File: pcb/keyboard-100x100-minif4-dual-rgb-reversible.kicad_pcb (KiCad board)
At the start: 2 copper layers, 100 x 100 mm, 96 parts, among them J1 TRRS, J2 TRRS, J3 Conn_01x04_Female, U1 MiniF4, U2 SN74LVC1T45DBV

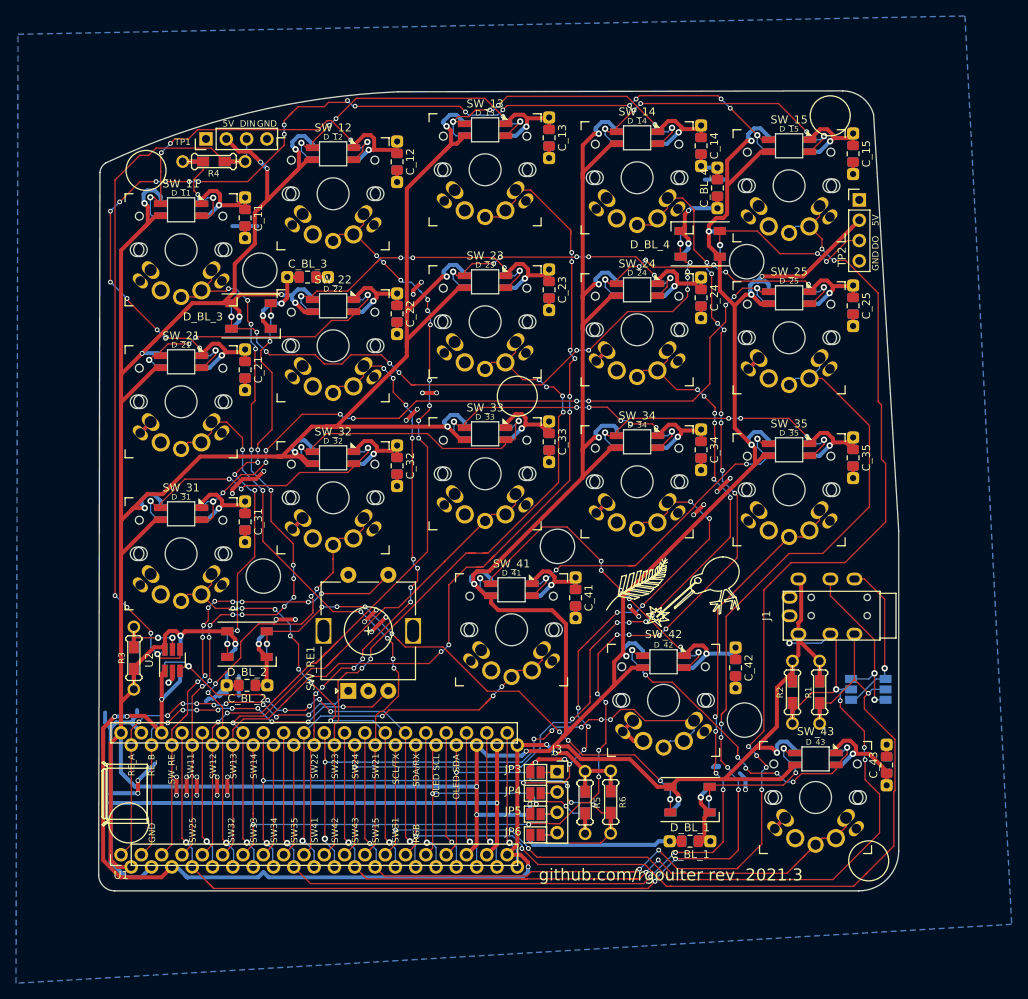
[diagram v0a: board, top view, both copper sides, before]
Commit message: Kicad: update schematic with M2 mounting holes
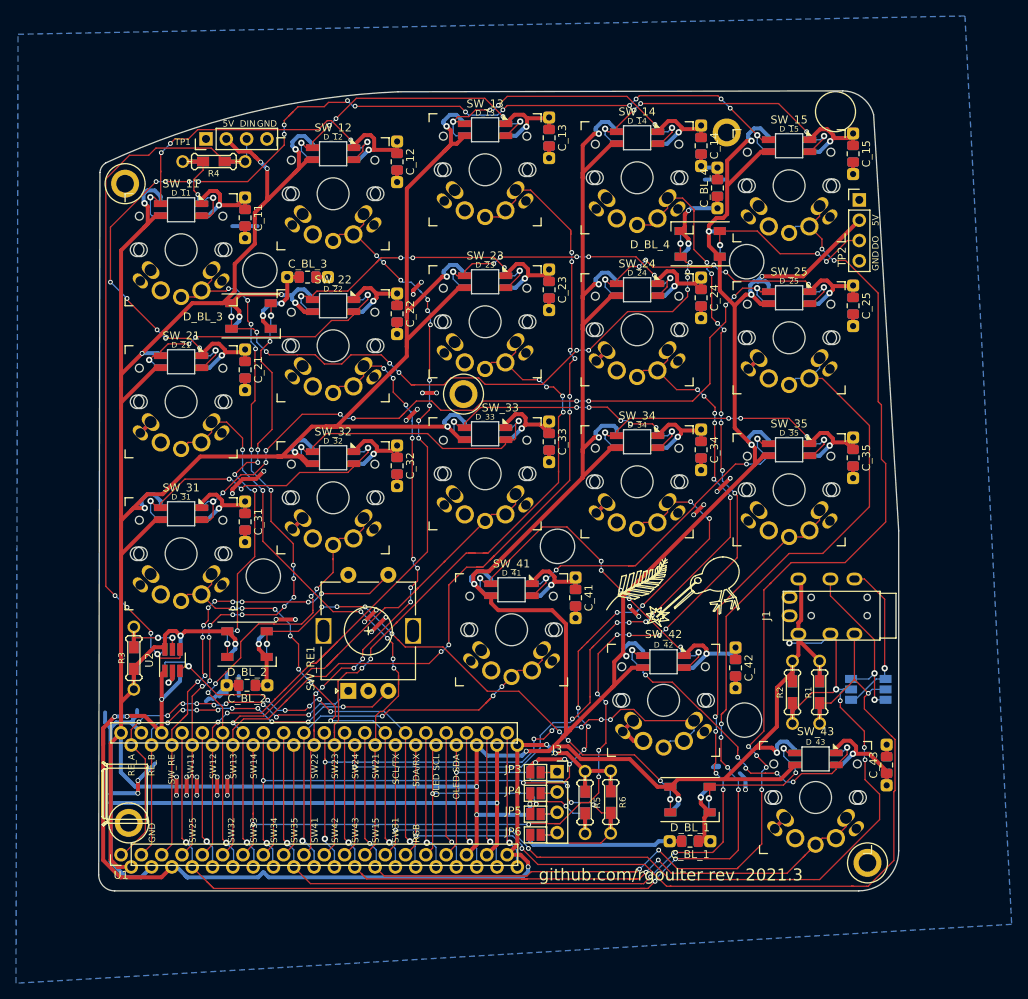
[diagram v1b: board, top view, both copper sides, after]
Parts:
- added H11: MountingHole, MountingHole:MountingHole_2.2mm_M2_ISO7380_Pad, F.Cu at (178.5, 55.2)
- added H12: MountingHole, MountingHole:MountingHole_2.2mm_M2_ISO7380_Pad, F.Cu at (103.3, 61.6)
- added H13: MountingHole, MountingHole:MountingHole_2.2mm_M2_ISO7380_Pad, F.Cu at (145.6, 87.9)
- added H14: MountingHole, MountingHole:MountingHole_2.2mm_M2_ISO7380_Pad, F.Cu at (103.8, 141.5)
- added H15: MountingHole, MountingHole:MountingHole_2.2mm_M2_ISO7380_Pad, F.Cu at (196.1, 146.5)
- moved H4 6.73 mm to (145.6, 87.9)
- moved H1 3.10 mm to (103.3, 61.6)
- moved H3 0.84 mm to (192.1, 52.6)
- moved H5 0.29 mm to (196.1, 146.5)
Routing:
- net /RGB_DIN_5V: track 86.1 -> 87.8 mm
- net /RE_A: track 47.1 -> 48.7 mm
- net /DOUT_1: track 127.1 -> 125.9 mm, vias 23 -> 21
- net /SCL_TX: track 123.8 -> 122.8 mm
- net /DOUT_2: track 95.2 -> 96.2 mm
- net /SDA_RX: track 117.9 -> 118.8 mm
- net Net-(D_BL_3-Pad4): track 79.4 -> 80.1 mm

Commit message: kicad: update keyboard for rev2021.4
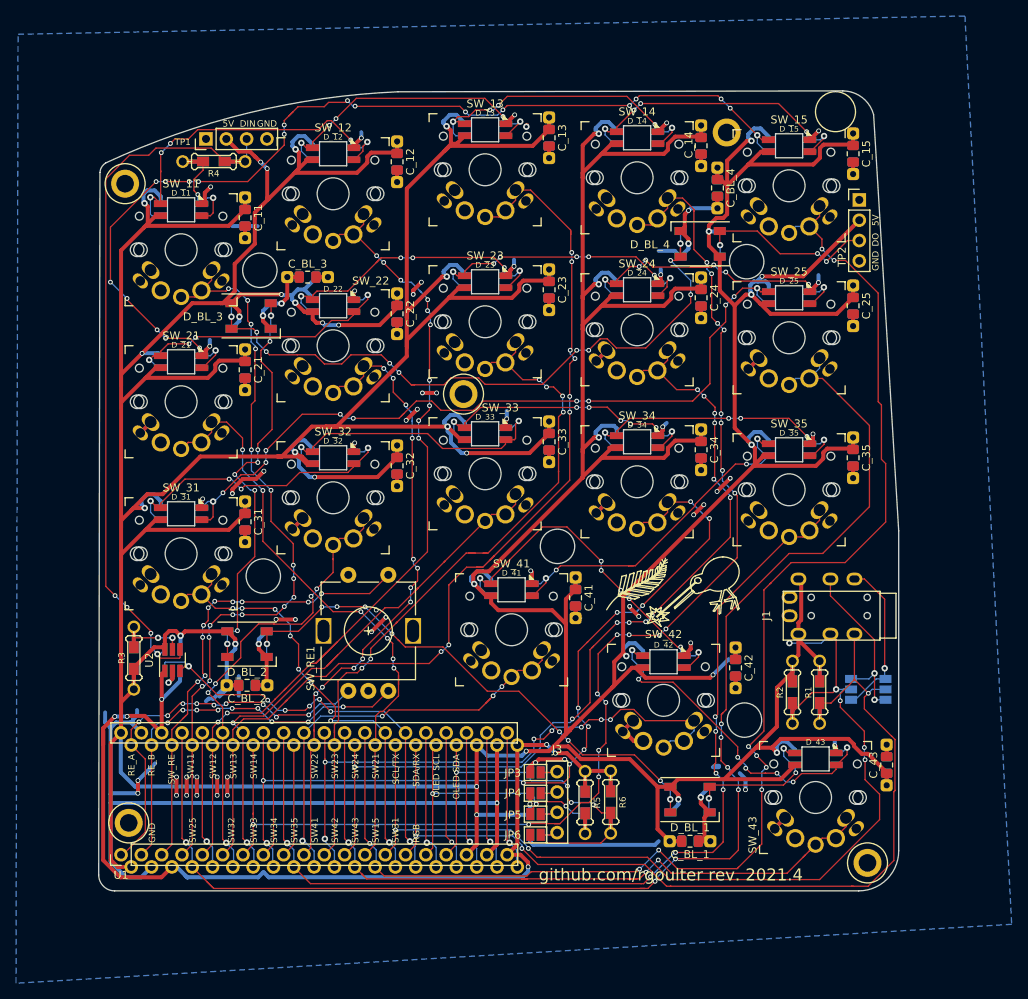
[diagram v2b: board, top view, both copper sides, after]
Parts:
- SW_RE1: footprint Rotary_Encoder:RotaryEncoder_Alps_EC11E-Switch_Vertical_H20mm -> ProjectLocal:RotaryEncoder_Alps_EC11E-Switch_Vertical_H20mm_Reversible
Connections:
- C_11 pad 2: Net-(C_11-Pad2) -> /5V
- C_12 pad 2: Net-(C_12-Pad2) -> /5V
- C_13 pad 2: Net-(C_13-Pad2) -> /5V
- C_14 pad 2: Net-(C_14-Pad2) -> /5V
- C_15 pad 2: Net-(C_15-Pad2) -> /5V
- C_21 pad 2: Net-(C_21-Pad2) -> /5V
- C_22 pad 2: Net-(C_22-Pad2) -> /5V
- C_23 pad 2: Net-(C_23-Pad2) -> /5V
- C_24 pad 2: Net-(C_24-Pad2) -> /5V
- C_25 pad 2: Net-(C_25-Pad2) -> /5V
- C_31 pad 2: Net-(C_31-Pad2) -> /5V
- C_32 pad 2: Net-(C_32-Pad2) -> /5V
- C_33 pad 2: Net-(C_33-Pad2) -> /5V
- C_34 pad 2: Net-(C_34-Pad2) -> /5V
- C_35 pad 2: Net-(C_35-Pad2) -> /5V
- C_41 pad 2: Net-(C_41-Pad2) -> /5V
- C_42 pad 2: Net-(C_42-Pad2) -> /5V
- C_43 pad 2: Net-(C_43-Pad2) -> /5V
- C_BL_1 pad 1: /GND -> /5V
- C_BL_1 pad 2: Net-(C_BL_1-Pad2) -> /GND
- C_BL_2 pad 1: /GND -> /5V
- C_BL_2 pad 2: Net-(C_BL_2-Pad2) -> /GND
- C_BL_3 pad 1: /GND -> /5V
- C_BL_3 pad 2: Net-(C_BL_3-Pad2) -> /GND
- C_BL_4 pad 1: /GND -> /5V
- C_BL_4 pad 2: Net-(C_BL_4-Pad2) -> /GND
- D_11 pad 3: Net-(C_11-Pad2) -> /GND
- D_12 pad 3: Net-(C_12-Pad2) -> /GND
- D_13 pad 3: Net-(C_13-Pad2) -> /GND
- D_14 pad 3: Net-(C_14-Pad2) -> /GND
- D_15 pad 3: Net-(C_15-Pad2) -> /GND
- D_21 pad 3: Net-(C_21-Pad2) -> /GND
- D_22 pad 3: Net-(C_22-Pad2) -> /GND
- D_23 pad 3: Net-(C_23-Pad2) -> /GND
- D_24 pad 3: Net-(C_24-Pad2) -> /GND
- D_25 pad 3: Net-(C_25-Pad2) -> /GND
- D_31 pad 3: Net-(C_31-Pad2) -> /GND
- D_32 pad 3: Net-(C_32-Pad2) -> /GND
- D_33 pad 3: Net-(C_33-Pad2) -> /GND
- D_34 pad 3: Net-(C_34-Pad2) -> /GND
- D_35 pad 3: Net-(C_35-Pad2) -> /GND
- D_41 pad 3: Net-(C_41-Pad2) -> /GND
- D_42 pad 3: Net-(C_42-Pad2) -> /GND
- D_43 pad 3: Net-(C_43-Pad2) -> /GND
- D_BL_1 pad 1: Net-(C_BL_1-Pad2) -> /GND
- D_BL_2 pad 1: Net-(C_BL_2-Pad2) -> /GND
- D_BL_3 pad 1: Net-(C_BL_3-Pad2) -> /GND
- D_BL_4 pad 1: Net-(C_BL_4-Pad2) -> /GND
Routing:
- net /5V: track 822.8 -> 1091.6 mm, vias 31 -> 36
- net /GND: track 207.7 -> 261.1 mm, vias 37 -> 60
- net Net-(C_43-Pad2): track 12.9 -> 0.00 mm, vias 1 -> 0
- net Net-(C_42-Pad2): track 11.6 -> 0.00 mm, vias 1 -> 0
- net Net-(C_11-Pad2): track 11.3 -> 0.00 mm, vias 1 -> 0
- net Net-(C_33-Pad2): track 11.2 -> 0.00 mm, vias 1 -> 0
- net Net-(C_23-Pad2): track 11.2 -> 0.00 mm, vias 1 -> 0
- net Net-(C_12-Pad2): track 11.2 -> 0.00 mm, vias 1 -> 0
- net Net-(C_24-Pad2): track 11.0 -> 0.00 mm, vias 1 -> 0
- net Net-(C_41-Pad2): track 10.9 -> 0.00 mm, vias 1 -> 0
- net Net-(C_22-Pad2): track 10.8 -> 0.00 mm, vias 1 -> 0
- net Net-(C_35-Pad2): track 10.8 -> 0.00 mm, vias 1 -> 0
- net Net-(C_BL_4-Pad2): track 10.7 -> 0.00 mm, vias 2 -> 0
- net Net-(C_32-Pad2): track 10.7 -> 0.00 mm, vias 1 -> 0
- net Net-(C_25-Pad2): track 10.5 -> 0.00 mm, vias 1 -> 0
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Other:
- board text added: "A"
- board text added: "B"
- board text added: "github.com/rgoulter rev. 2021.4"
- board text removed: "github.com/rgoulter rev. 2021.3"

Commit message: kicad: update for rev2021.5
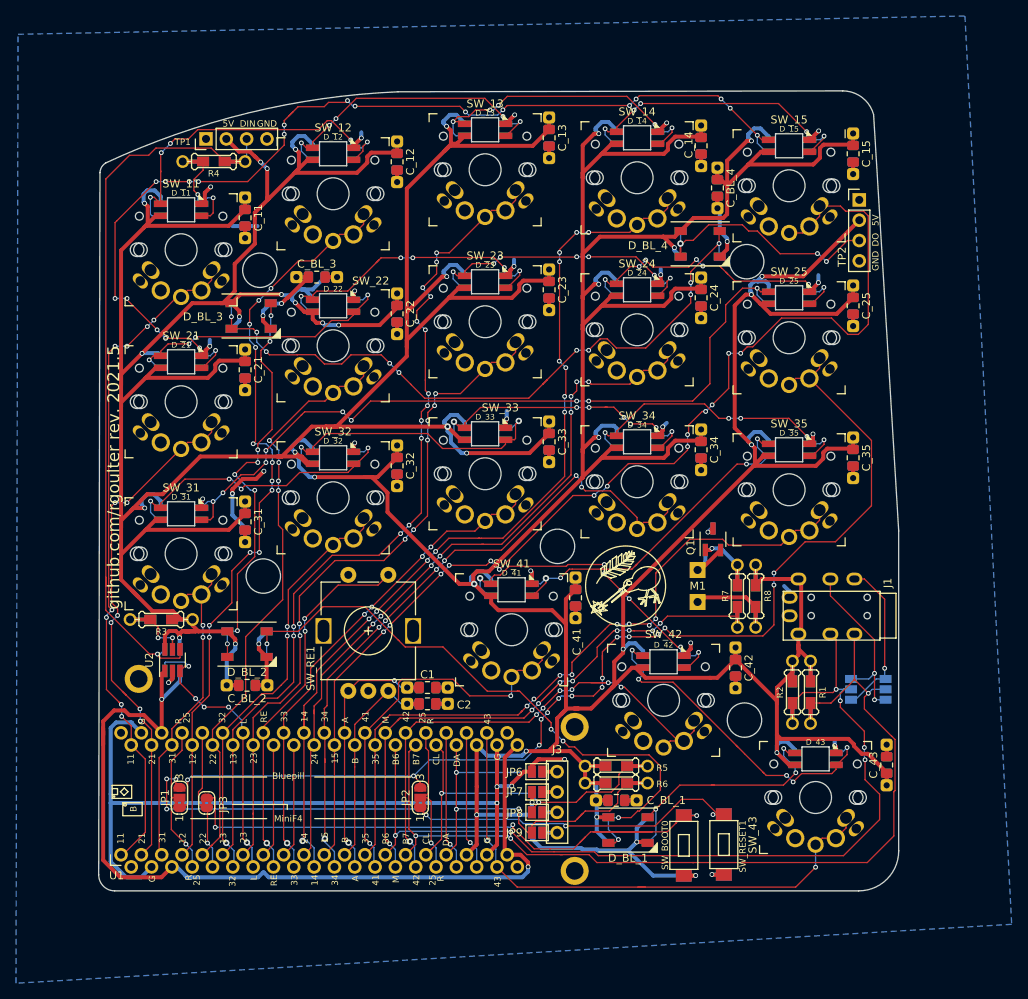
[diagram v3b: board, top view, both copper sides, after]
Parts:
- removed H14, H15: MountingHole, MountingHole:MountingHole_2.2mm_M2_ISO7380_Pad
- added C1: 100nF, ProjectLocal:C_0805_2012Metric_Pad1.18x1.45mm_HandSolder_Dual, F.Cu at (141.1, 124.6)
- added C2: 100nF, ProjectLocal:C_0805_2012Metric_Pad1.18x1.45mm_HandSolder_Dual, F.Cu at (141.1, 126.6)
- added JP1: SolderJumper_3_Bridged12, Jumper:SolderJumper-3_P1.3mm_Bridged2Bar12_RoundedPad1.0x1.5mm_NumberLabels, F.Cu at (110.1, 138.3)
- added JP2: SolderJumper_3_Bridged12, Jumper:SolderJumper-3_P1.3mm_Bridged2Bar12_RoundedPad1.0x1.5mm_NumberLabels, F.Cu at (140.2, 138.3)
- added JP3: SolderJumper_2_Bridged, Jumper:SolderJumper-2_P1.3mm_Bridged2Bar_RoundedPad1.0x1.5mm, F.Cu at (113.5, 139.0)
- added M1: Motor_DC, ProjectLocal:Mini_DC_Motor, F.Cu at (165.9, 111.9)
- added Q1: Q_NPN_BCE, ProjectLocal:SOT-23_Handsoldering_Reversible, F.Cu at (176.8, 106.0)
- added R7: 500R, ProjectLocal:Resistor-Hybrid, F.Cu at (179.8, 113.2)
- added R8: 500R, ProjectLocal:Resistor-Hybrid, F.Cu at (182.1, 113.2)
- added SW_BOOT0: SW_Push, ProjectLocal:SW_Push_SPST_3x6mm, F.Cu at (173.1, 140.5)
- added SW_RESET1: SW_Push, ProjectLocal:SW_Push_SPST_3x6mm, F.Cu at (178.1, 140.4)
- U1: value MiniF4 -> BluePill_or_MiniF4; footprint ProjectLocal:WeAct_MiniF4_ZigZag -> ProjectLocal:DIP40_Reversible_ZigZag
- moved H1 125.6 mm to (196.1, 146.3)
- moved H11 100.3 mm to (105.0, 123.5)
- moved H5 92.2 mm to (104.0, 141.9)
- moved H12 88.1 mm to (159.5, 129.5)
- moved H2 63.4 mm to (140.1, 89.5)
- moved H13 61.2 mm to (159.5, 147.5)
- moved H4 49.8 mm to (103.5, 61.3)
- moved C_BL_1 10.5 mm to (164.7, 138.7)
- moved D_BL_1 8.63 mm to (166.2, 142.4)
- moved R5 5.99 mm to (164.7, 134.4), turned to 180 degrees
- moved R3 5.92 mm to (107.8, 116.1), turned to 180 degrees
- moved R6 2.48 mm to (164.7, 136.5), turned to 180 degrees
- moved C_BL_3 1.14 mm to (127.3, 73.3)
- moved R1 1.14 mm to (189.0, 125.2)
- moved JP10 0.34 mm to (154.8, 142.7)
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- renumbered JP7 to JP10, JP8 to JP11, JP9 to JP12, JP10 to JP13, JP1 to JP4, JP2 to JP5, JP3 to JP6, JP4 to JP7, JP5 to JP8, JP6 to JP9
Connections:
- R5 pad 1: /3V3 -> /5V
- R6 pad 1: /3V3 -> /5V
- U1 pad 1: Net-(U1-Pad1) -> /SW11
- U1 pad 10: /RGB_DIN_3V3 -> /SW24
- U1 pad 11: /SW31 -> /SW15
- U1 pad 12: /SW15 -> /RE_B
- U1 pad 13: /SW43 -> /SW35
- U1 pad 14: /SW42 -> /SCL_TX
- U1 pad 15: /SW41 -> /SDA_RX
- U1 pad 16: /SW35 -> /OLED_SCL
- U1 pad 17: /SW34 -> /OLED_SDA
- U1 pad 18: /SW33 -> /5V
- U1 pad 19: /SW32 -> /GND
- U1 pad 2: Net-(U1-Pad2) -> /SW21
- U1 pad 20: Net-(U1-Pad20) -> /3V3
- U1 pad 21: /SW25 -> (no net)
- U1 pad 25: /RE_A -> /NC_or_BOOT0
- U1 pad 26: /RE_B -> /SW32
- U1 pad 27: /SW_RE -> /RGB_DIN_3V3
- U1 pad 28: /SW11 -> /SW_RE
- U1 pad 29: /SW12 -> /SW33
- U1 pad 3: Net-(U1-Pad3) -> /SW31
- U1 pad 30: /SW13 -> /SW14
- U1 pad 31: /SW14 -> /SW34
- U1 pad 32: Net-(U1-Pad32) -> /RE_A
- U1 pad 33: Net-(U1-Pad33) -> /SW41
- U1 pad 38: /SW22 -> Net-(U1-Pad38)
- U1 pad 39: /SW23 -> /SW43
- U1 pad 4: Net-(U1-Pad4) -> /SW12
- U1 pad 40: /SW24 -> (no net)
- U1 pad 7: Net-(U1-Pad7) -> /SW23
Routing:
- net /5V: track 1091.6 -> 1001.9 mm, vias 36 -> 34
- net /RESET: track 0.00 -> 82.7 mm, vias 0 -> 6
- net /BOOT0: track 0.00 -> 78.3 mm, vias 0 -> 3
- net /MOTOR_PWM: track 0.00 -> 71.5 mm, vias 0 -> 9
- net /GND: track 261.1 -> 214.7 mm, vias 60 -> 33
- net /SW14: track 156.8 -> 116.2 mm, vias 18 -> 13
- net /SW35: track 122.8 -> 89.2 mm, vias 7 -> 8
- net /SW25: track 171.5 -> 140.5 mm, vias 7 -> 15
- net /SW15: track 171.1 -> 140.7 mm, vias 9 -> 14
- net /SW34: track 111.7 -> 83.8 mm, vias 11 -> 7
- net /RE_B: track 49.3 -> 25.9 mm, vias 9 -> 0
- net /RGB_DIN_3V3: track 55.2 -> 35.7 mm, vias 7 -> 5
- net /RESET_or_SW25: track 0.00 -> 19.4 mm, vias 0 -> 1
- net /SW43: track 88.4 -> 69.1 mm, vias 3 -> 2
- net /SW25_or_RESET: track 0.00 -> 18.9 mm, vias 0 -> 1
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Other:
- board text added: "11"
- board text added: "12"
- board text added: "13"
- board text added: "14"
- board text added: "15"
- board text added: "21"
- board text added: "22"
- board text added: "23"
- board text added: "24"
- board text added: "25"
- board text added: "31"
- board text added: "32"
- board text added: "33"
- board text added: "34"
- board text added: "35"
- board text added: "41"
- board text added: "42"
- board text added: "43"
- board text added: "B6"
- board text added: "B7"
- board text added: "Bluepill"
- board text added: "CL"
- board text added: "DA"
- board text added: "G"
- board text added: "L"
- board text added: "M"
- board text added: "MiniF4"
- board text added: "R"
- board text added: "RE"
- board text added: "github.com/rgoulter rev. 2021.5"
- board text removed: "OLED SCL"
- board text removed: "OLED SDA"
- board text removed: "RE_A"
- board text removed: "RE_B"
- board text removed: "RGB"
- board text removed: "SCL/TX"
- board text removed: "SDA/RX"
- board text removed: "SW11"
- board text removed: "SW12"
- board text removed: "SW13"
- board text removed: "SW14"
- board text removed: "SW15"
- board text removed: "SW21"
- board text removed: "SW22"
- board text removed: "SW23"
- board text removed: "SW24"
- board text removed: "SW25"
- board text removed: "SW31"
- board text removed: "SW32"
- board text removed: "SW33"
- board text removed: "SW34"
- board text removed: "SW35"
- board text removed: "SW41"
- board text removed: "SW42"
- board text removed: "SW43"
- board text removed: "SW_RE"
- board text removed: "github.com/rgoulter rev. 2021.4"

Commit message: Kicad: fix ordering of pin numbers in DIP40_Reversible_ZigZag footprint
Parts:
- U1: value BluePill_or_MiniF4 -> BluePill_or_MiniF4_DIP40
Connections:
- U1 pad 22: /GND -> /SW43
- U1 pad 23: /3V3 -> Net-(U1-Pad23)
- U1 pad 24: /RESET_or_SW25 -> Net-(U1-Pad24)
- U1 pad 25: /NC_or_BOOT0 -> /SW25_or_RESET
- U1 pad 26: /SW32 -> /SW42
- U1 pad 27: /RGB_DIN_3V3 -> /MOTOR_PWM
- U1 pad 28: /SW_RE -> /SW41
- U1 pad 29: /SW33 -> /RE_A
- U1 pad 30: /SW14 -> /SW34
- U1 pad 31: /SW34 -> /SW14
- U1 pad 32: /RE_A -> /SW33
- U1 pad 33: /SW41 -> /SW_RE
- U1 pad 34: /MOTOR_PWM -> /RGB_DIN_3V3
- U1 pad 35: /SW42 -> /SW32
- U1 pad 36: /SW25_or_RESET -> /NC_or_BOOT0
- U1 pad 37: Net-(U1-Pad37) -> /RESET_or_SW25
- U1 pad 38: Net-(U1-Pad38) -> /3V3
- U1 pad 39: /SW43 -> /GND
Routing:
- net Net-(U1-Pad38): track 17.3 -> 0.00 mm, vias 1 -> 0
- net Net-(U1-Pad23): track 0.00 -> 17.3 mm, vias 0 -> 1
- net Net-(U1-Pad37): track 17.3 -> 0.00 mm, vias 1 -> 0
- net Net-(U1-Pad24): track 0.00 -> 17.3 mm, vias 0 -> 1

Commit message: Kicad: update the footprint names to "_Reversible" in x-1 minif4-36
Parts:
- C1, C2, C_11, C_12, C_13, C_14, C_15, C_21, C_22, C_23, C_24, C_25, C_31, C_32, C_33, C_34, C_35, C_41, C_42, C_43, C_BL_1, C_BL_2, C_BL_3, C_BL_4: footprint ProjectLocal:C_0805_2012Metric_Pad1.18x1.45mm_HandSolder_Dual -> ProjectLocal:C_0805_2012Metric_Pad1.18x1.45mm_HandSolder_Dual_Reversible
- R1, R2, R3, R4, R5, R6, R7, R8: footprint ProjectLocal:Resistor-Hybrid -> ProjectLocal:Resistor-Hybrid_Reversible
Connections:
- U1 pad 21: (no net) -> Net-(U1-Pad21)
- U1 pad 40: (no net) -> /GND_or_5V
